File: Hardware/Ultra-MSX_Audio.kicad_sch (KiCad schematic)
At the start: 26 parts, among them J16 Waveblaster_header_02x13, J17 X2GS_midi_card, U23 S29GL128S90TFI010, U24 FXMA108, U25 FXMA108, U26 FXMA108, U27 FXMA108, U4 YM2610, U9 DAC_YM3016

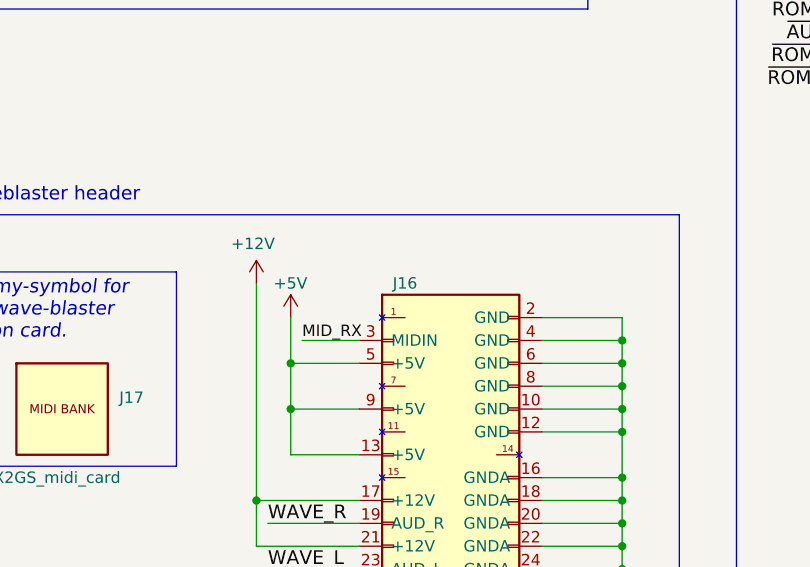
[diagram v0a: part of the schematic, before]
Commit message: Updated the readme, silenced multiple errors in Kicad regarding simulation-files.
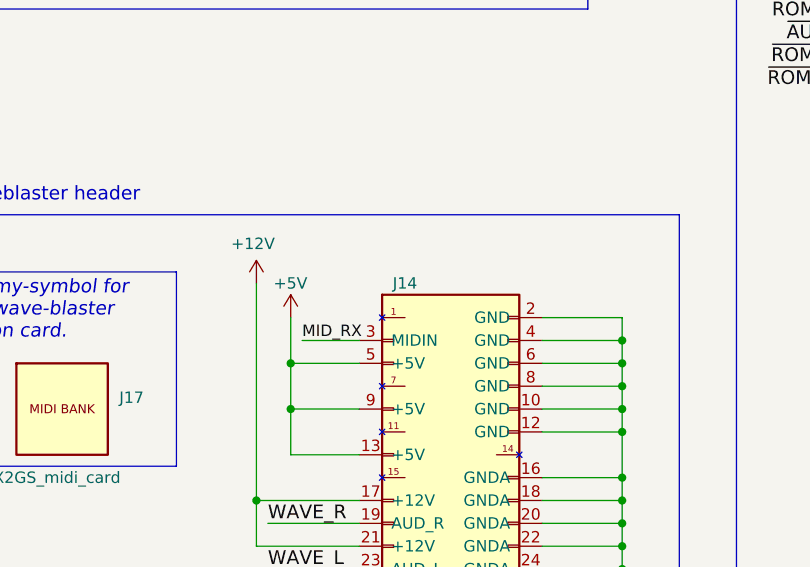
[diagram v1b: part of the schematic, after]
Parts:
- J17: MPN (none) -> X2GS; Manufacturer (none) -> Serdashop
- renumbered J16 to J14
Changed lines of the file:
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@@
       (effects (font (size 1.524 1.524)) hide)
+    )
+    (property "Sim.Enable" "0" (at 318.77 147.32 0)
+      (effects (font (size 1.27 1.27)) hide)
     )
     (pin "13")
@@
     )
     (property "Description" "Combined SSG, ADPCM and FM-synth" (at 101.6 82.55 0)
+      (effects (font (size 1.27 1.27)) hide)
+    )
+    (property "Sim.Enable" "0" (at 50.8 77.47 0)
       (effects (font (size 1.27 1.27)) hide)
     )
@@
       (effects (font (size 1.27 1.27)) hide)
     )
+    (property "Sim.Enable" "0" (at 228.6 67.31 0)
+      (effects (font (size 1.27 1.27)) hide)
+    )
     (pin "1")
     (pin "11")
@@
       (effects (font (size 1.27 1.27)) hide)
     )
+    (property "Sim.Enable" "0" (at 138.43 95.25 0)
+      (effects (font (size 1.27 1.27)) hide)
+    )
     (pin "1")
     (pin "10")
@@
       (effects (font (size 1.27 1.27)) hide)
     )
+    (property "Sim.Enable" "0" (at 138.43 44.45 0)
+      (effects (font (size 1.27 1.27)) hide)
+    )
     (pin "1")
     (pin "10")
@@
       (effects (font (size 1.27 1.27)) hide)
     )
+    (property "Manufacturer" "Serdashop" (at 48.26 179.07 0)
+      (effects (font (size 1.27 1.27)) hide)
+    )
+    (property "MPN" "X2GS" (at 46.355 181.61 0)
+      (effects (font (size 1.27 1.27)) hide)
+    )
+    (property "Sim.Enable" "0" (at 45.72 189.23 0)
+      (effects (font (size 1.27 1.27)) hide)
+    )
     (instances
       (project "Ultra-MSX"
@@
   (symbol (lib_id "Ultra-MSX:Waveblaster_header_02x13") (at 81.28 191.77 0) (unit 1)
     (in_bom yes) (on_board yes) (dnp no)
-    (property "Reference" "J16" (at 76.2 172.72 0)
+    (property "Reference" "J14" (at 76.2 172.72 0)
       (effects (font (size 1.27 1.27)))
     )
@@
     )
     (property "Datasheet" "~" (at 73.66 171.45 0)
+      (effects (font (size 1.27 1.27)) hide)
+    )
+    (property "Sim.Enable" "0" (at 81.28 191.77 0)
       (effects (font (size 1.27 1.27)) hide)
     )
@@
       (project "Ultra-MSX"
         (path "/b7496a40-6116-4192-b413-2a22be4b5f9f/00000000-0000-0000-0000-00005bd9dbb3"
-          (reference "J16") (unit 1)
+          (reference "J14") (unit 1)
         )
       )
@@
     )
     (property "Datasheet" "http://www.onsemi.com/pub/Collateral/FXMA108-D.pdf" (at 138.43 190.5 0)
+      (effects (font (size 1.27 1.27)) hide)
+    )
+    (property "Sim.Enable" "0" (at 138.43 191.77 0)
       (effects (font (size 1.27 1.27)) hide)
     )
@@
       (effects (font (size 1.27 1.27)) hide)
     )
+    (property "Sim.Enable" "0" (at 138.43 143.51 0)
+      (effects (font (size 1.27 1.27)) hide)
+    )

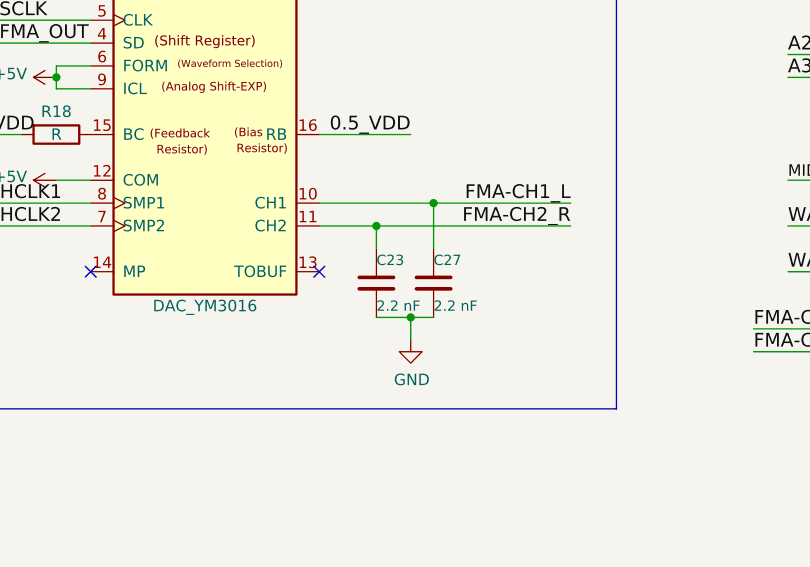
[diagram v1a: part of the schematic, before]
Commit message: Added a 3D-model for the SDRAM-module. Prepping the design for a fork using a single, more modern FPGA.
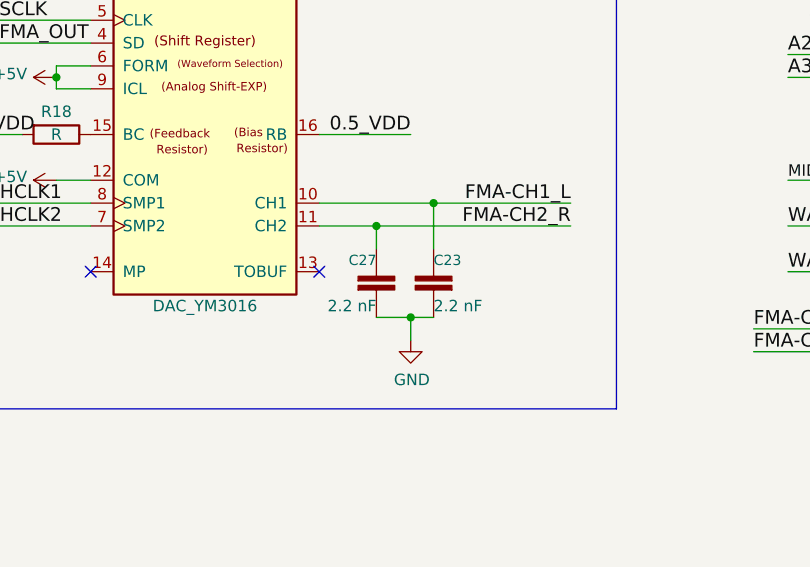
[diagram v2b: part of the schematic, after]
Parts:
- removed C23, C27: C_K222K10X7RF5UH5, LRJ:C_Rect_L3.6mm_W2.3mm_P5.08mm, symbol LRJ-parts:C_GRM1885C1H222
- added C23, C27: GCM2165C2A222FA16D, Capacitor_SMD:C_0805_2012Metric_Pad1.18x1.45mm_HandSolder, symbol LRJ-parts:C_GCM2165C2A222FA16D
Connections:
- net FMA-CH1_L: now also C23.1
- net FMA-CH2_R: now also C27.1
- net GND: now also C23.2, C27.2
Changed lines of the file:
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@@
-    )
-  )
-  (symbol (lib_id "LRJ-parts:C_GRM1885C1H222") (at 344.17 163.83 0) (unit 1)
-    (in_bom yes) (on_board yes) (dnp no)
-    (property "Reference" "C27" (at 344.17 161.29 0)
-      (effects (font (size 1.143 1.143)) (justify left))
-    )
-    (property "Value" "C_K222K10X7RF5UH5" (at 347.98 163.195 0)
-      (effects (font (size 1.143 1.143)) (justify left) hide)
-    )
-    (property "Footprint" "LRJ:C_Rect_L3.6mm_W2.3mm_P5.08mm" (at 354.33 161.29 0)
-      (effects (font (size 0.508 0.508)) hide)
-    )
-    (property "Datasheet" "https://search.murata.co.jp/Ceramy/image/img/A01X/G101/ENG/GRM1885C1H222JA01-01.pdf" (at 372.11 171.45 0)
-      (effects (font (size 1.27 1.27)) hide)
-    )
-    (property "Manufacturer" "Murata Electronics" (at 354.33 151.13 0)
-      (effects (font (size 1.27 1.27)) hide)
-    )
-    (property "MPN" "GRM1885C1H222JA01D" (at 356.87 148.59 0)
-      (effects (font (size 1.27 1.27)) hide)
-    )
-    (property "Capacity" "2.2 nF" (at 344.17 166.37 0)
-      (effects (font (size 1.143 1.143)) (justify left))
-    )
-    (property "Type" "SMD" (at 349.25 153.67 0)
-      (effects (font (size 1.27 1.27)) hide)
-    )
-    (property "Voltage rating" "50V" (at 347.98 167.005 0)
-      (effects (font (size 1.27 1.27)) (justify left) hide)
-    )
-    (property "Temperature coefficient" "C0G" (at 349.25 158.75 0)
-      (effects (font (size 1.27 1.27)) hide)
-    )
-    (property "Status" "Active" (at 350.52 167.64 0)
-      (effects (font (size 1.27 1.27)) hide)
-    )
-    (property "Description" "2200 pF ±5% 50V Ceramic Capacitor C0G, NP0 0603 (1608 Metric)" (at 379.73 156.21 0)
-      (effects (font (size 1.27 1.27)) hide)
-    )
-    (pin "1")
-    (pin "2")
-    (instances
-      (project "Ultra-MSX"
-        (path "/b7496a40-6116-4192-b413-2a22be4b5f9f/00000000-0000-0000-0000-00005bd9dbb3"
-          (reference "C27") (unit 1)
-        )
-      )
     )
   )
@@
     )
   )
-  (symbol (lib_id "LRJ-parts:C_GRM1885C1H222") (at 337.82 163.83 0) (unit 1)
-    (in_bom yes) (on_board yes) (dnp no)
-    (property "Reference" "C23" (at 337.82 161.29 0)
-      (effects (font (size 1.143 1.143)) (justify left))
-    )
-    (property "Value" "C_K222K10X7RF5UH5" (at 341.63 163.195 0)
-      (effects (font (size 1.143 1.143)) (justify left) hide)
-    )
-    (property "Footprint" "LRJ:C_Rect_L3.6mm_W2.3mm_P5.08mm" (at 347.98 161.29 0)
-      (effects (font (size 0.508 0.508)) hide)
-    )
-    (property "Datasheet" "https://search.murata.co.jp/Ceramy/image/img/A01X/G101/ENG/GRM1885C1H222JA01-01.pdf" (at 365.76 171.45 0)
-      (effects (font (size 1.27 1.27)) hide)
-    )
-    (property "Manufacturer" "Murata Electronics" (at 347.98 151.13 0)
-      (effects (font (size 1.27 1.27)) hide)
-    )
-    (property "MPN" "GRM1885C1H222JA01D" (at 350.52 148.59 0)
+  (symbol (lib_id "LRJ-parts:C_GCM2165C2A222FA16D") (at 337.82 165.1 0) (unit 1)
+    (in_bom yes) (on_board yes) (dnp no)
+    (property "Reference" "C27" (at 337.82 161.29 0)
+      (effects (font (size 1.143 1.143)) (justify right))
+    )
+    (property "Value" "GCM2165C2A222FA16D" (at 334.01 163.83 0)
+      (effects (font (size 1.143 1.143)) (justify right) hide)
+    )
+    (property "Footprint" "Capacitor_SMD:C_0805_2012Metric_Pad1.18x1.45mm_HandSolder" (at 373.38 162.56 0)
+      (effects (font (size 1.27 1.27)) hide)
+    )
+    (property "Datasheet" "https://search.murata.co.jp/Ceramy/image/img/A01X/G101/ENG/GCM2165C2A222FA16-01.pdf" (at 390.906 175.641 0)
+      (effects (font (size 1.27 1.27)) hide)
+    )
+    (property "Mouser datasheet" "https://www.mouser.se/datasheet/2/281/GCM2165C2A222FA16_01-1967706.pdf" (at 382.016 166.751 0)
       (effects (font (size 1.27 1.27)) hide)
     )
     (property "Capacity" "2.2 nF" (at 337.82 166.37 0)
-      (effects (font (size 1.143 1.143)) (justify left))
-    )
-    (property "Type" "SMD" (at 342.9 153.67 0)
-      (effects (font (size 1.27 1.27)) hide)
-    )
-    (property "Voltage rating" "50V" (at 341.63 167.005 0)
-      (effects (font (size 1.27 1.27)) (justify left) hide)
-    )
-    (property "Temperature coefficient" "C0G" (at 342.9 158.75 0)
-      (effects (font (size 1.27 1.27)) hide)
-    )
-    (property "Status" "Active" (at 344.17 167.64 0)
-      (effects (font (size 1.27 1.27)) hide)
-    )
-    (property "Description" "2200 pF ±5% 50V Ceramic Capacitor C0G, NP0 0603 (1608 Metric)" (at 373.38 156.21 0)
-      (effects (font (size 1.27 1.27)) hide)
-    )
-    (pin "1")
-    (pin "2")
-    (instances
-      (project "Ultra-MSX"
-        (path "/b7496a40-6116-4192-b413-2a22be4b5f9f/00000000-0000-0000-0000-00005bd9dbb3"
-          (reference "C23") (unit 1)
+      (effects (font (size 1.27 1.27)) (justify right))
+    )
+    (property "Type" "SMD" (at 345.44 154.94 0)
+      (effects (font (size 1.27 1.27)) hide)
+    )
+    (property "Voltage rating" "100V" (at 345.44 152.4 0)
+      (effects (font (size 1.27 1.27)) hide)
+    )
+    (property "Status" "Active" (at 346.456 171.831 0)
+      (effects (font (size 1.27 1.27)) hide)
+    )
+    (property "Manufacturer" "Murata" (at 345.44 147.32 0)
+      (effects (font (size 1.27 1.27)) hide)
+    )
+    (property "MPN" "GCM2165C2A222FA16D" (at 353.06 149.86 0)
+      (effects (font (size 1.27 1.27)) hide)
+    )
+    (pin "1")
+    (pin "2")
+    (instances
+      (project "Ultra-MSX"
+        (path "/b7496a40-6116-4192-b413-2a22be4b5f9f/00000000-0000-0000-0000-00005bd9dbb3"
+          (reference "C27") (unit 1)
         )
       )
@@
         )
       )
+    )
+  )
+  (symbol (lib_id "LRJ-parts:C_GCM2165C2A222FA16D") (at 344.17 165.1 0) (mirror y) (unit 1)
+    (in_bom yes) (on_board yes) (dnp no)
+    (property "Reference" "C23" (at 344.17 161.29 0)
+      (effects (font (size 1.143 1.143)) (justify right))
+    )
+    (property "Value" "GCM2165C2A222FA16D" (at 347.98 163.83 0)
+      (effects (font (size 1.143 1.143)) (justify right) hide)
+    )
+    (property "Footprint" "Capacitor_SMD:C_0805_2012Metric_Pad1.18x1.45mm_HandSolder" (at 308.61 162.56 0)
+      (effects (font (size 1.27 1.27)) hide)
+    )
+    (property "Datasheet" "https://search.murata.co.jp/Ceramy/image/img/A01X/G101/ENG/GCM2165C2A222FA16-01.pdf" (at 291.084 175.641 0)
+      (effects (font (size 1.27 1.27)) hide)
+    )
+    (property "Mouser datasheet" "https://www.mouser.se/datasheet/2/281/GCM2165C2A222FA16_01-1967706.pdf" (at 299.974 166.751 0)
+      (effects (font (size 1.27 1.27)) hide)
+    )
+    (property "Capacity" "2.2 nF" (at 344.17 166.37 0)
+      (effects (font (size 1.27 1.27)) (justify right))
+    )
+    (property "Type" "SMD" (at 336.55 154.94 0)
+      (effects (font (size 1.27 1.27)) hide)
+    )
+    (property "Voltage rating" "100V" (at 336.55 152.4 0)
+      (effects (font (size 1.27 1.27)) hide)
+    )
+    (property "Status" "Active" (at 335.534 171.831 0)
+      (effects (font (size 1.27 1.27)) hide)
+    )
+    (property "Manufacturer" "Murata" (at 336.55 147.32 0)
+      (effects (font (size 1.27 1.27)) hide)
+    )
+    (property "MPN" "GCM2165C2A222FA16D" (at 328.93 149.86 0)
+      (effects (font (size 1.27 1.27)) hide)
+    )
+    (pin "1")
+    (pin "2")
+    (instances
+      (project "Ultra-MSX"
+        (path "/b7496a40-6116-4192-b413-2a22be4b5f9f/00000000-0000-0000-0000-00005bd9dbb3"
+          (reference "C23") (unit 1)
+        )
+      )
